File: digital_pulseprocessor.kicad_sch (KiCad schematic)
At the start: 22 parts, among them U300 SN74LV221AD, U301 SN74LV221AD, U305 74AC151M n.b.

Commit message: Changes in BOM. Add JLCpcb Part Nr
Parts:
- C300: footprint (none) -> Capacitor_SMD:C_0805_2012Metric_Pad1.18x1.45mm_HandSolder; JLCBasicPart (none) -> Basic; JLCPartNr (none) -> C1814; JLCType (none) -> CL21C330JBANNNC; OriginalType (none) -> TCC0805COG330J500BT
- C303: footprint (none) -> Capacitor_SMD:C_0805_2012Metric_Pad1.18x1.45mm_HandSolder; JLCBasicPart (none) -> Basic; JLCPartNr (none) -> C46653; JLCType (none) -> CL21B102KBCNNNC; OriginalType (none) -> 0805B102K500CT
- C304: footprint (none) -> Capacitor_SMD:C_0805_2012Metric_Pad1.18x1.45mm_HandSolder; JLCBasicPart (none) -> Basic; JLCPartNr (none) -> C49678; JLCType (none) -> CC0805KRX7R9BB104; OriginalType (none) -> FN21X104K500PXG
- R300, R303: footprint (none) -> Resistor_SMD:R_0805_2012Metric_Pad1.20x1.40mm_HandSolder; JLCBasicPart (none) -> Basic; JLCPartNr (none) -> C17513; JLCType (none) -> 0805W8F1001T5E; OriginalType (none) -> AR05FTDW1001
- R304: footprint (none) -> Resistor_SMD:R_0805_2012Metric_Pad1.20x1.40mm_HandSolder; JLCBasicPart (none) -> Basic; JLCPartNr (none) -> C17709; JLCType (none) -> 0805W8F4703T5E; OriginalType (none) -> RS-05K4703FT
- R306, R310, R311: footprint (none) -> Resistor_SMD:R_0805_2012Metric_Pad1.20x1.40mm_HandSolder; JLCBasicPart (none) -> Basic; JLCPartNr (none) -> C17738; JLCType (none) -> 0805W8F510JT5E; OriginalType (none) -> CR0805J80510G
- R702, R703: footprint (none) -> Resistor_SMD:R_0805_2012Metric_Pad1.20x1.40mm_HandSolder; JLCBasicPart (none) -> Basic; JLCPartNr (none) -> C17437; JLCType (none) -> 0805W8F1200T5E; OriginalType (none) -> CR0805J80121G

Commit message: Minor Fixes
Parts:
- JP300: symbol Device:Jumper_NC_Small -> Jumper:Jumper_2_Open
- JP301, JP302: symbol Device:Jumper_NO_Small -> Jumper:Jumper_2_Open
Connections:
- no-connect marks 5 -> 13

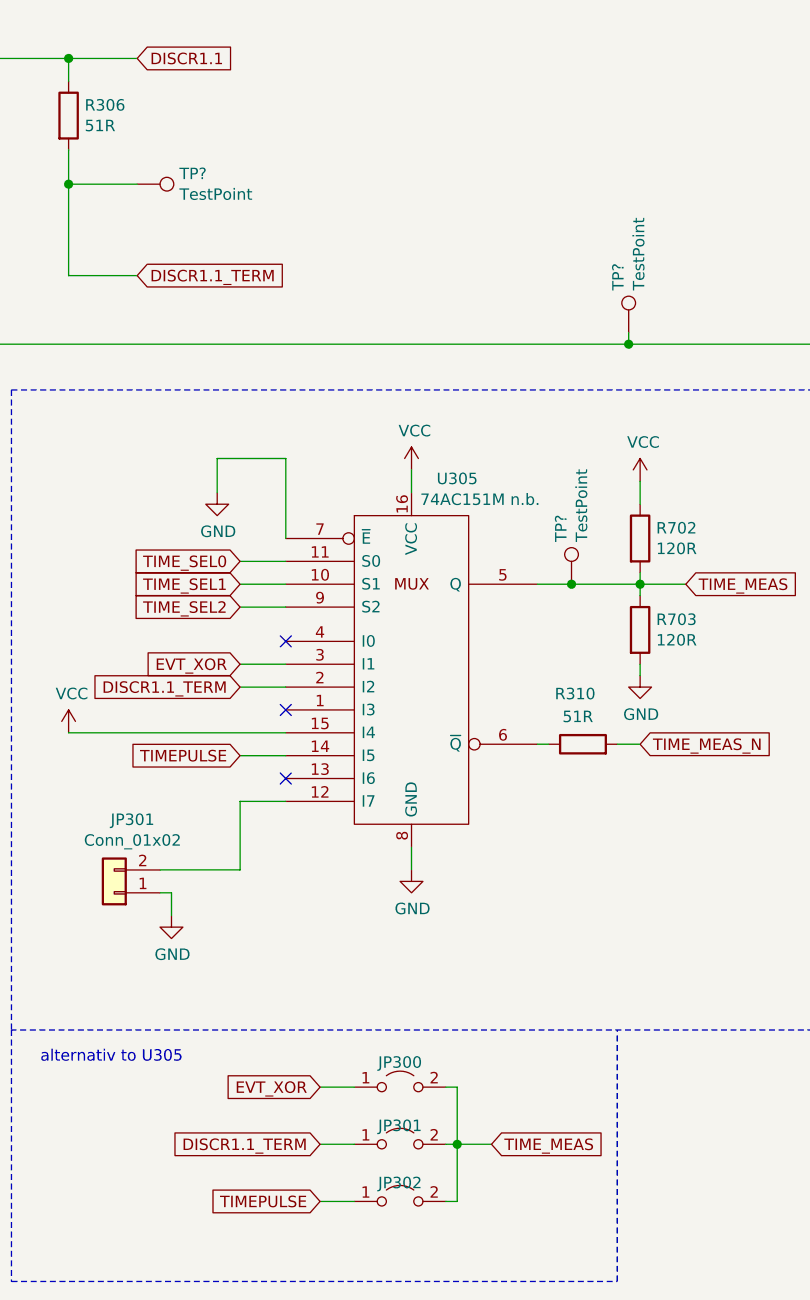
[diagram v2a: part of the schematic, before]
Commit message: working on BOM. Small Fixes in Schematics
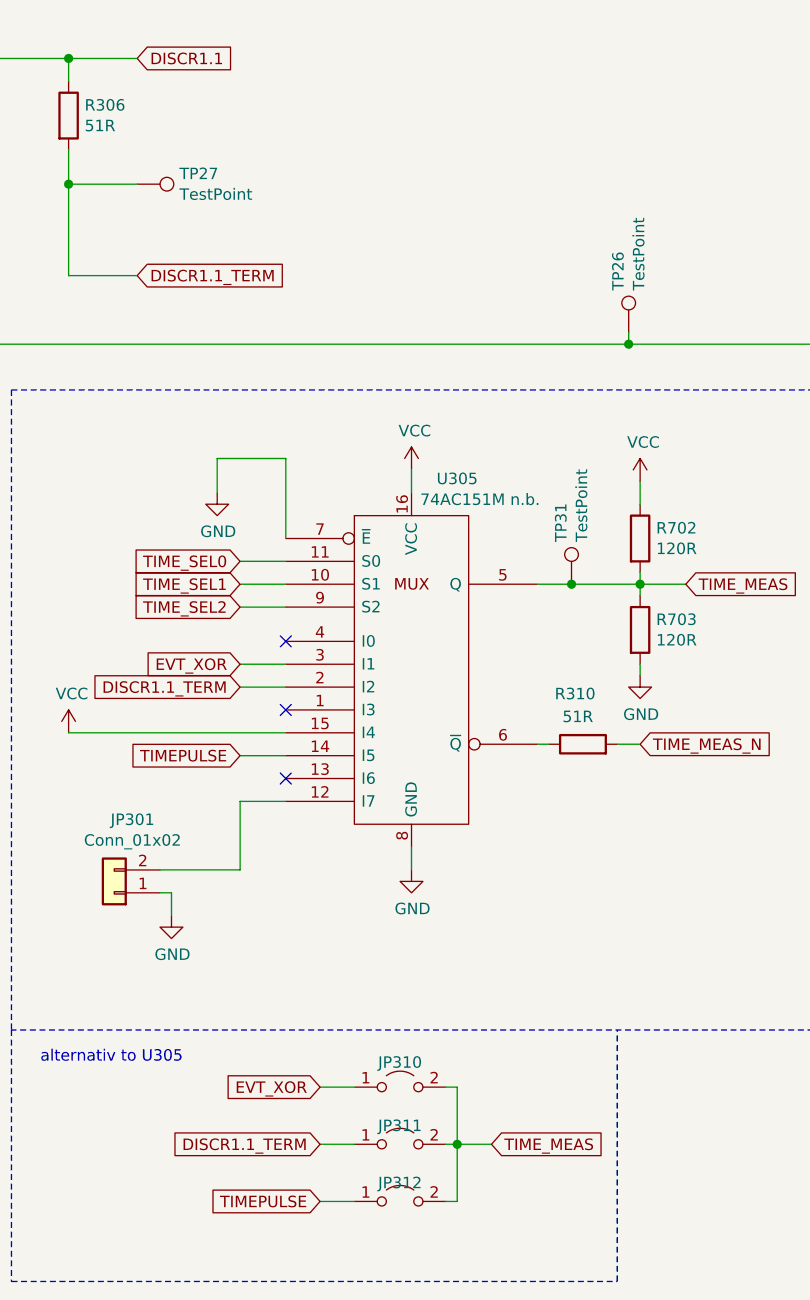
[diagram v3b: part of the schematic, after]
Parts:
- U300, U301: footprint (none) -> Package_SO:SOIC-16W_7.5x10.3mm_P1.27mm
- U305: symbol 74xx_IEEE:74151 -> muonpi-kicad-library:74AC151M
- gave numbers to parts that had none: 3
- renumbered JP300 to JP310, JP301 to JP311, JP302 to JP312
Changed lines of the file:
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@@
   (symbol (lib_id "Connector:TestPoint") (at 121.92 71.12 270) (unit 1)
     (in_bom yes) (on_board yes)
-    (property "Reference" "TP?" (id 0) (at 126.6191 69.9706 90)
+    (property "Reference" "TP27" (id 0) (at 126.6191 69.9706 90)
       (effects (font (size 1.27 1.27)) (justify left))
     )
@@
   (symbol (lib_id "Connector:TestPoint") (at 170.18 115.57 0) (unit 1)
     (in_bom yes) (on_board yes)
-    (property "Reference" "TP?" (id 0) (at 169.0306 110.8709 90)
+    (property "Reference" "TP31" (id 0) (at 169.0306 110.8709 90)
       (effects (font (size 1.27 1.27)) (justify left))
     )
@@
   (symbol (lib_id "Connector:TestPoint") (at 176.53 87.63 0) (unit 1)
     (in_bom yes) (on_board yes)
-    (property "Reference" "TP?" (id 0) (at 175.3806 82.9309 90)
+    (property "Reference" "TP26" (id 0) (at 175.3806 82.9309 90)
       (effects (font (size 1.27 1.27)) (justify left))
     )
@@
   (symbol (lib_id "Jumper:Jumper_2_Open") (at 151.13 171.45 0) (unit 1)
     (in_bom yes) (on_board yes)
-    (property "Reference" "JP300" (id 0) (at 151.13 168.7068 0))
+    (property "Reference" "JP310" (id 0) (at 151.13 168.7068 0))
     (property "Value" "Jumper_NC_Small" (id 1) (at 151.13 168.4782 0)
       (effects (font (size 1.27 1.27)) hide)
@@
   (symbol (lib_id "Jumper:Jumper_2_Open") (at 151.13 177.8 0) (unit 1)
     (in_bom yes) (on_board yes)
-    (property "Reference" "JP301" (id 0) (at 151.13 175.7426 0))
+    (property "Reference" "JP311" (id 0) (at 151.13 175.7426 0))
     (property "Value" "Jumper_NO_Small" (id 1) (at 151.13 175.514 0)
       (effects (font (size 1.27 1.27)) hide)
@@
   (symbol (lib_id "Jumper:Jumper_2_Open") (at 151.13 184.15 0) (unit 1)
     (in_bom yes) (on_board yes)
-    (property "Reference" "JP302" (id 0) (at 151.13 182.0926 0))
+    (property "Reference" "JP312" (id 0) (at 151.13 182.0926 0))
     (property "Value" "Jumper_NO_Small" (id 1) (at 151.13 181.864 0)
       (effects (font (size 1.27 1.27)) hide)
@@
     (property "Reference" "U300" (id 0) (at 57.15 155.5814 0))
     (property "Value" "SN74LV221AD" (id 1) (at 58.42 157.8801 0))
-    (property "Footprint" "" (id 2) (at 67.31 167.64 0)
+    (property "Footprint" "Package_SO:SOIC-16W_7.5x10.3mm_P1.27mm" (id 2) (at 67.31 167.64 0)
       (effects (font (size 1.27 1.27)) hide)
     )
@@
     (property "Reference" "U301" (id 0) (at 82.55 155.5814 0))
     (property "Value" "SN74LV221AD" (id 1) (at 85.09 157.8801 0))
-    (property "Footprint" "" (id 2) (at 93.98 167.64 0)
+    (property "Footprint" "Package_SO:SOIC-16W_7.5x10.3mm_P1.27mm" (id 2) (at 93.98 167.64 0)
       (effects (font (size 1.27 1.27)) hide)
     )
@@
     (property "Reference" "U300" (id 0) (at 71.12 71.7614 0))
     (property "Value" "SN74LV221AD" (id 1) (at 71.12 74.0664 0))
-    (property "Footprint" "" (id 2) (at 71.12 62.23 0)
+    (property "Footprint" "Package_SO:SOIC-16W_7.5x10.3mm_P1.27mm" (id 2) (at 71.12 62.23 0)
       (effects (font (size 1.27 1.27)) hide)
     )
@@
     (property "Reference" "U300" (id 0) (at 71.12 131.4514 0))
     (property "Value" "SN74LV221AD" (id 1) (at 71.12 133.7501 0))
-    (property "Footprint" "" (id 2) (at 71.12 121.92 0)
+    (property "Footprint" "Package_SO:SOIC-16W_7.5x10.3mm_P1.27mm" (id 2) (at 71.12 121.92 0)
       (effects (font (size 1.27 1.27)) hide)
     )
@@
     (property "Reference" "U301" (id 0) (at 222.25 100.965 0))
     (property "Value" "SN74LV221AD" (id 1) (at 222.25 103.2701 0))
-    (property "Footprint" "" (id 2) (at 222.25 91.44 0)
+    (property "Footprint" "Package_SO:SOIC-16W_7.5x10.3mm_P1.27mm" (id 2) (at 222.25 91.44 0)
       (effects (font (size 1.27 1.27)) hide)
     )
@@
     (property "Reference" "U301" (id 0) (at 242.57 137.795 0))
     (property "Value" "SN74LV221AD" (id 1) (at 242.57 140.1001 0))
-    (property "Footprint" "" (id 2) (at 242.57 128.27 0)
+    (property "Footprint" "Package_SO:SOIC-16W_7.5x10.3mm_P1.27mm" (id 2) (at 242.57 128.27 0)
       (effects (font (size 1.27 1.27)) hide)
     )
@@
     (pin "4")
   )
-  (symbol (lib_id "74xx_IEEE:74151") (at 152.4 124.46 0) (unit 1)
+  (symbol (lib_id "muonpi-kicad-library:74AC151M") (at 152.4 124.46 0) (unit 1)
     (in_bom yes) (on_board yes)
     (property "Reference" "U305" (id 0) (at 157.48 103.8606 0))

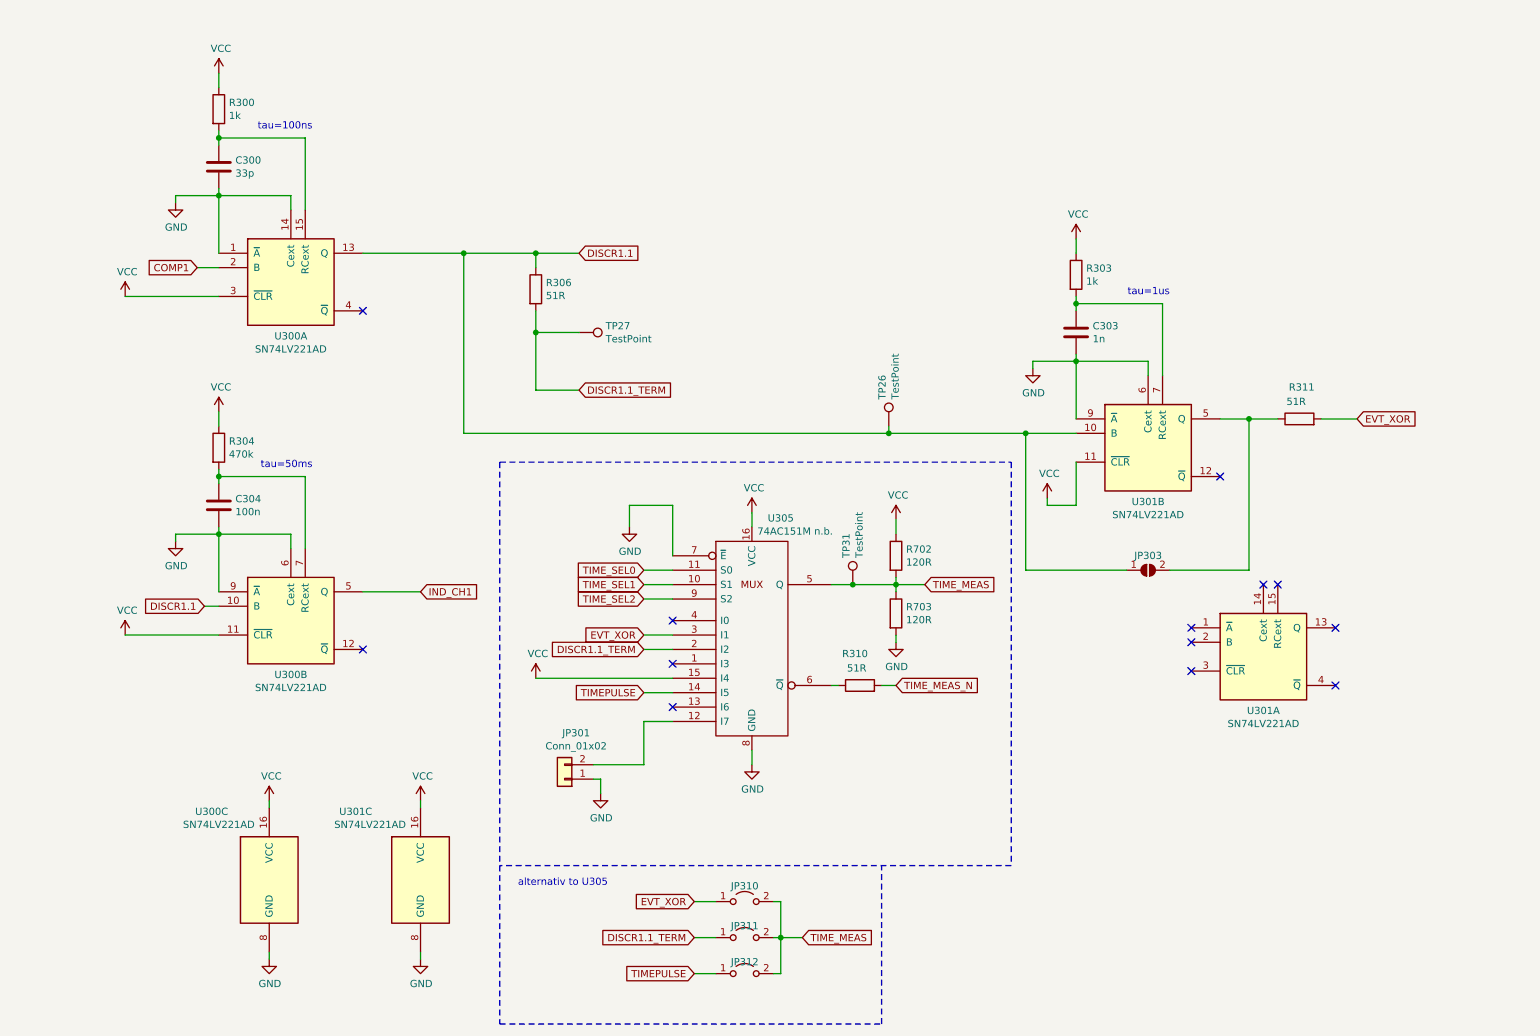
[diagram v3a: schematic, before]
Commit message: Footprints assigned. Testpoints added
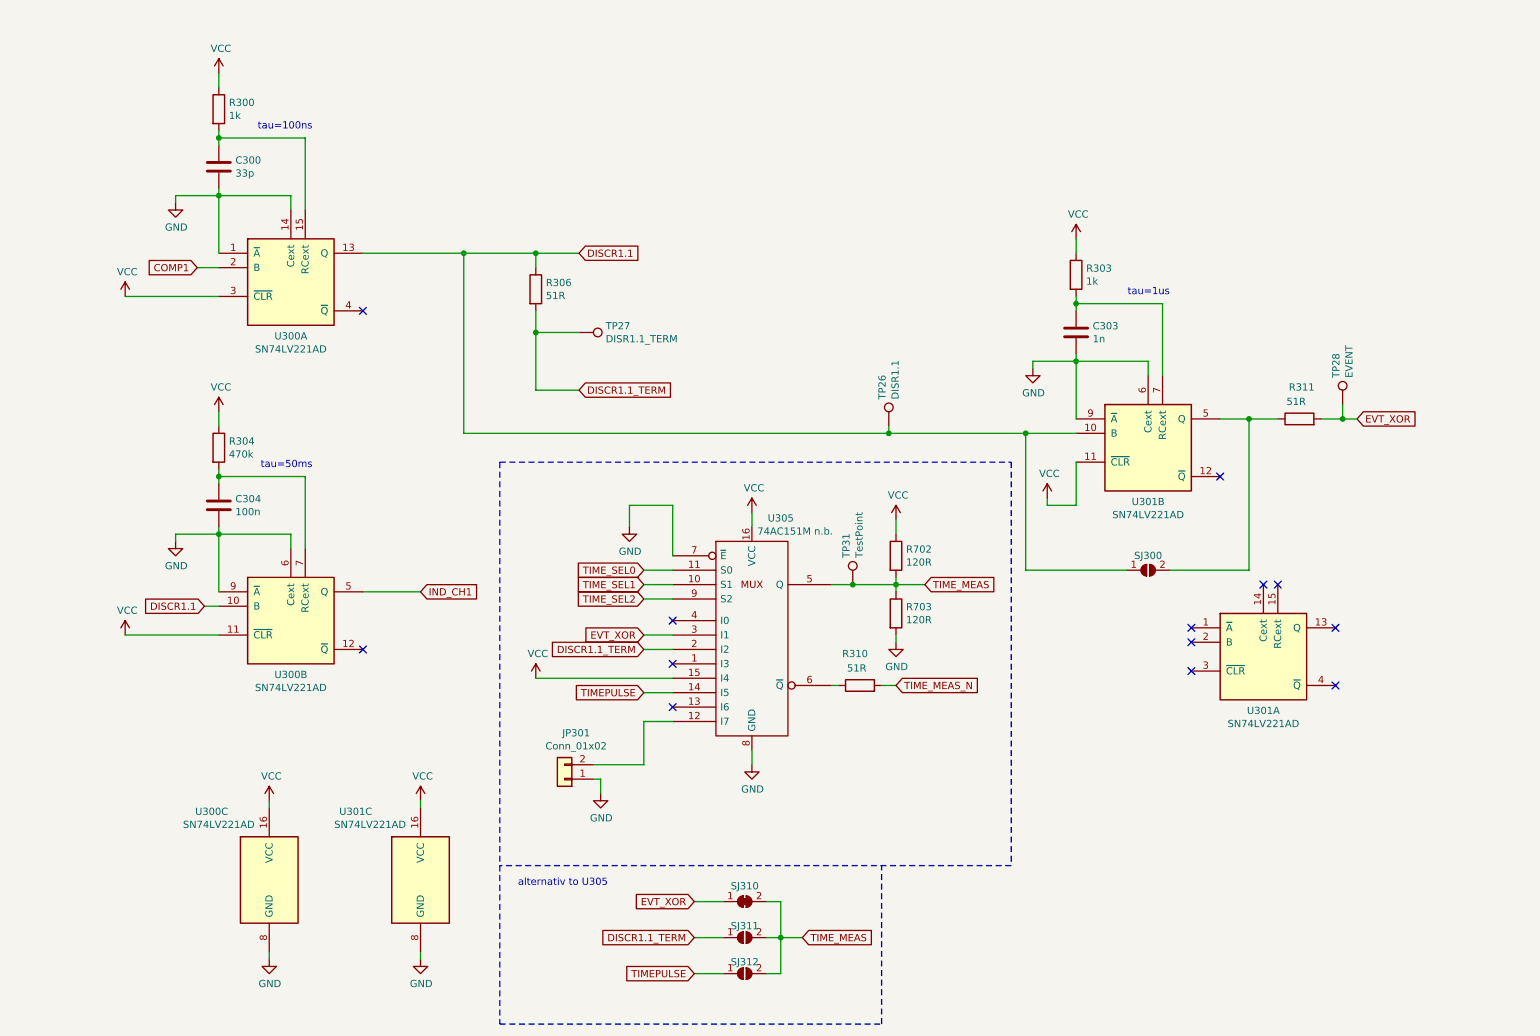
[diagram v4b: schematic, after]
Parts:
- added TP28: EVENT, TestPoint:TestPoint_THTPad_1.5x1.5mm_Drill0.7mm, symbol Connector:TestPoint
- JP301: footprint (none) -> Connector_PinHeader_2.54mm:PinHeader_1x02_P2.54mm_Vertical
- SJ300: renamed from JP303; footprint (none) -> Jumper:SolderJumper-2_P1.3mm_Open_Pad1.0x1.5mm
- SJ310: renamed from JP310; footprint (none) -> Jumper:SolderJumper-2_P1.3mm_Bridged_Pad1.0x1.5mm; symbol Jumper:Jumper_2_Open -> Jumper:SolderJumper_2_Bridged; now left out of the parts list
- SJ311: renamed from JP311; footprint (none) -> Jumper:SolderJumper-2_P1.3mm_Open_Pad1.0x1.5mm; symbol Jumper:Jumper_2_Open -> Jumper:SolderJumper_2_Open; now left out of the parts list
- SJ312: renamed from JP312; footprint (none) -> Jumper:SolderJumper-2_P1.3mm_Open_Pad1.0x1.5mm; symbol Jumper:Jumper_2_Open -> Jumper:SolderJumper_2_Open; now left out of the parts list
- TP26: value TestPoint -> DISR1.1; footprint (none) -> TestPoint:TestPoint_THTPad_1.5x1.5mm_Drill0.7mm; now left out of the parts list
- TP27: value TestPoint -> DISR1.1_TERM; footprint (none) -> TestPoint:TestPoint_THTPad_1.5x1.5mm_Drill0.7mm; now left out of the parts list
- TP31: footprint (none) -> TestPoint:TestPoint_THTPad_1.5x1.5mm_Drill0.7mm; now left out of the parts list
- U300, U301: OriginalType (none) -> 595-SN74LV221ADR; Supplier (none) -> Mouser
- U305: footprint (none) -> Package_SO:SOP-16_3.9x9.9mm_P1.27mm; JLCBasicPart (none) -> -; OriginalType (none) -> 595-CD74AC151M96; Supplier (none) -> Mouser
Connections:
- net EVT_XOR: now also TP28.1

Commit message: Changed the position of the capacitor in the circuit diagram. Capacitors are now close to the components as on the circuit board.
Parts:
- added C564, C566: 100n, Capacitor_SMD:C_0805_2012Metric_Pad1.18x1.45mm_HandSolder, symbol Device:C
- added C570: 100n n.b., Capacitor_SMD:C_0805_2012Metric_Pad1.18x1.45mm_HandSolder, symbol Device:C
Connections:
- net GND: now also C564.2, C566.2, C570.2
- net VCC: now also C564.1, C566.1, C570.1
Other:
- moved on the sheet: U300C
